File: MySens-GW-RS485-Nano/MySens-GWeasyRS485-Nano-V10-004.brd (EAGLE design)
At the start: 74 x 34 mm, 43 parts, among them X7 1751264

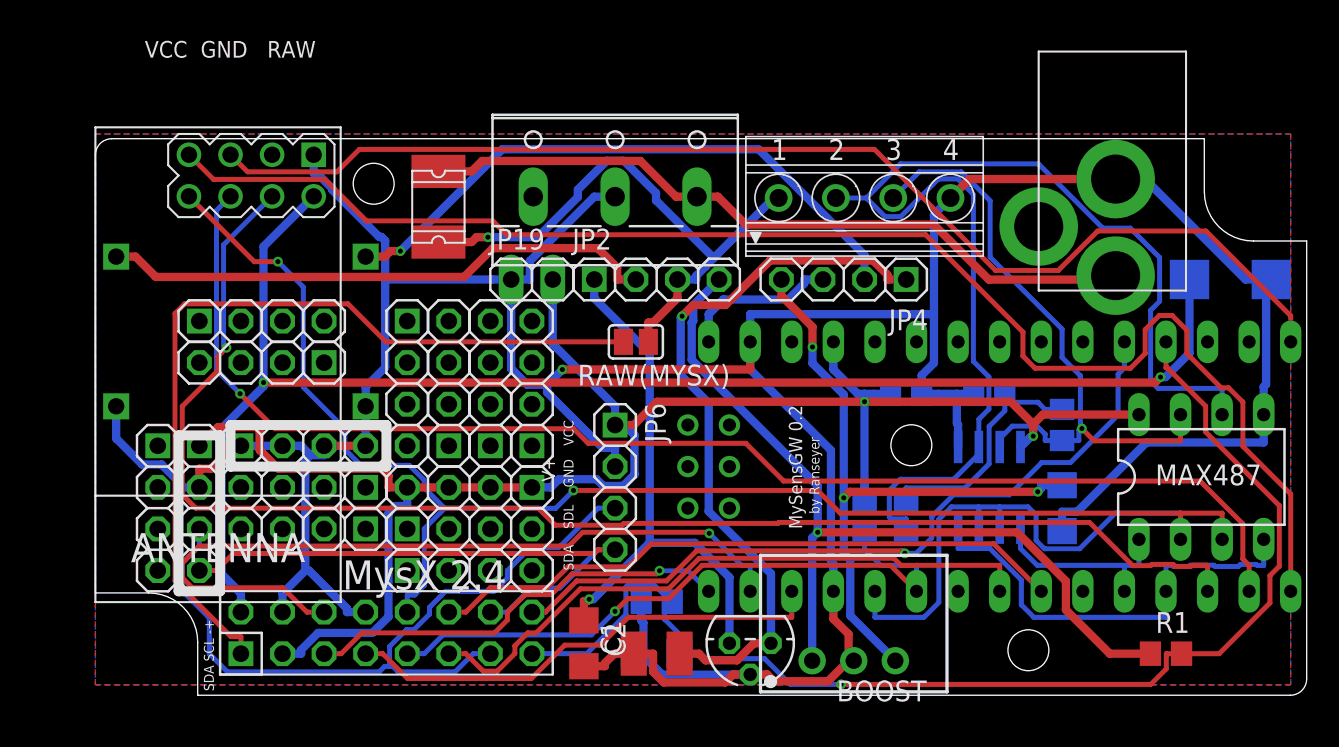
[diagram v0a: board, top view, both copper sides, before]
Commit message: Some new easyBoards
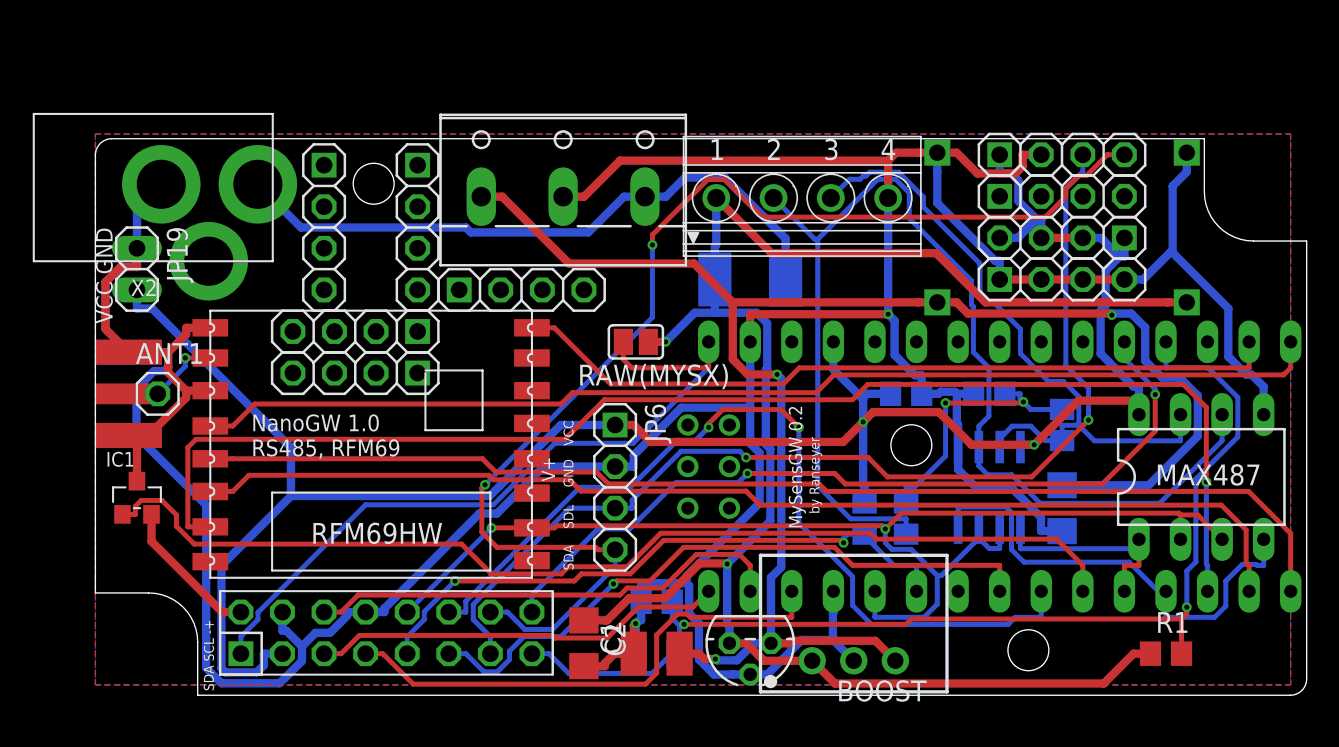
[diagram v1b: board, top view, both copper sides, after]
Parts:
- removed C3: 4,7, rcl:SMC_C
- removed JP17, JP18, JP2, JP4, JP5, JP7, JP9: (no value), pinhead-2:1X04-S
- removed NRF24L01+: WIRELESS-NRF24L01, diy-modules:WIRELESS-NRF24L01
- added ANT1: (no value), pinhead:1X01
- added IC1: ATSHA204A, Sensor:SOT23
- added RFM69W: RFM69HW, hoperf:RFM
- added X2: (no value), adafruit:SMA_EDGELAUNCH
- moved U$3 61.7 mm to (0.64, 31.1), turned to 90 degrees
- moved JP10 57.0 mm to (59.1, 33.0), turned to 0 degrees
- moved REG2 50.6 mm to (59.1, 28.6), turned to 0 degrees
- moved JP1 47.5 mm to (59.1, 25.4)
- moved JP15 41.5 mm to (59.1, 30.5)
- moved JP3 39.3 mm to (59.1, 27.9)
- moved JP19 24.1 mm to (2.54, 26.0), turned to 270 degrees
- moved JP16 23.4 mm to (19.7, 28.6)
- moved F1 19.6 mm to (40.0, 25.4), flipped to the bottom, turned to 180 degrees
- moved JP12 15.9 mm to (14.0, 28.6), turned to 270 degrees
- moved JP13 11.3 mm to (15.9, 22.2), turned to 180 degrees
- moved JP14 9.03 mm to (26.0, 24.8), turned to 0 degrees
- moved JP11 5.75 mm to (15.9, 19.7)
- moved X7 3.81 mm to (43.2, 30.5)
- moved REGULATED 3.18 mm to (28.6, 31.8)
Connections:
- removed net BOOSTIN: BOOST.1, JP2.4, R1.1
- removed net BOOSTOUT: BOOST.3, C5.2, JP4.4
- removed net CE: NRF24L01+.3
- removed net N$1: MYSX.1, RAW(MYSX).2
- removed net R1IN: C2.1, JP2.1, REG1.3
- removed net R1OUT: C1.1, JP4.1, REG1.1
- removed net R2IN: JP2.2, REG2.IN+
- removed net R2OUT: JP4.2, REG2.OUT+
- removed net RAW: JP4.3, U$2.RAW
- removed net REG: REGULATED.1
- removed net UREG: F1.P$1, JP2.3, RAW(MYSX).1, X7.1
- new net IN: BOOST.1, C2.1, F1.P$1, R1.1, RAW(MYSX).1, REG1.3, REG2.IN+, X7.1
- new net N$16: ANT1.1, RFM69W.ANT, X2.P
- new net OUT: BOOST.3, C1.1, C5.2, REG1.1, REG2.OUT+, REGULATED.1
- new net RW: MYSX.1, RAW(MYSX).2, U$2.RAW
- net 3.3V: now also IC1.2; no longer C3.+, NRF24L01+.2
- net 3V3: now also RFM69W.VCC
- net CSN: now also RFM69W.NSS; no longer NRF24L01+.4
- net D7: now also IC1.1
- net GND: now also IC1.3, RFM69W.GNDA, RFM69W.GNDB, X2.GND@1, X2.GND@2, X2.GND@3, X2.GND@4; no longer C3.-, NRF24L01+.1
- net IRQ: now also RFM69W.DIO0; no longer NRF24L01+.8
- net MISO: now also RFM69W.MISO; no longer NRF24L01+.7
- net MOSI: now also RFM69W.MOSI; no longer NRF24L01+.6
- net SCK: now also RFM69W.SCK; no longer NRF24L01+.5
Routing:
- net IN: track 0.00 -> 105.2 mm, vias 0 -> 2
- net OUT: track 0.00 -> 99.8 mm, vias 0 -> 3
- net 3.3V: track 90.0 -> 8.90 mm, vias 2 -> 0
- net D7: track 0.00 -> 65.0 mm
- net BOOSTIN: track 51.7 -> 0.00 mm, vias 1 -> 0
- net N$1: track 51.4 -> 0.00 mm
- net 3V3: track 0.00 -> 47.2 mm
- net IRQ: track 120.4 -> 73.9 mm
- net RW: track 0.00 -> 46.3 mm
- net R1OUT: track 44.2 -> 0.00 mm, vias 1 -> 0
- net BOOSTOUT: track 40.0 -> 0.00 mm, vias 3 -> 0
- net A4: track 35.1 -> 74.8 mm, vias 0 -> 2
- net R2OUT: track 37.4 -> 0.00 mm, vias 1 -> 0
- net GND: track 235.6 -> 270.7 mm, vias 1 -> 2
- net UREG: track 35.0 -> 0.00 mm, vias 1 -> 0
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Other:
- board text added: "NanoGW 1.0 RS485, RFM69"
- board text added: "VCC GND"
- board text removed: "MysX 2.4"
- board text removed: "VCC GND RAW"
